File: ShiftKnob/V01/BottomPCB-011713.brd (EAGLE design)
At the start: 35.6 x 37.8 mm, 39 parts, among them IC2 7805DT, Q1 16MHz, Q2 MOSFET-NCHANNELSMD, Q3 MOSFET-NCHANNELSMD, Q4 MOSFET-NCHANNELSMD, Q5 MOSFET-NCHANNELSMD, Q6 MOSFET-NCHANNELSMD, U1 ATMEGA328

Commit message: adjust silk screen layer for large font size.
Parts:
- moved U$11 5.91 mm to (16.8, 25.8)
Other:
- board text added: "1-28-13"
- board text removed: "1-25-13"
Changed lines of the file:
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@@
 <grid distance="0.001" unitdist="inch" unit="inch" style="lines" multiple="1" display="yes" altdistance="0.025" altunitdist="inch" altunit="inch"/>
 <layers>
-<layer number="1" name="Top" color="4" fill="1" visible="yes" active="yes"/>
-<layer number="16" name="Bottom" color="1" fill="1" visible="yes" active="yes"/>
+<layer number="1" name="Top" color="4" fill="1" visible="no" active="yes"/>
+<layer number="16" name="Bottom" color="1" fill="1" visible="no" active="yes"/>
 <layer number="17" name="Pads" color="2" fill="1" visible="yes" active="yes"/>
 <layer number="18" name="Vias" color="2" fill="1" visible="yes" active="yes"/>
 <layer number="19" name="Unrouted" color="6" fill="1" visible="yes" active="yes"/>
 <layer number="20" name="Dimension" color="15" fill="1" visible="yes" active="yes"/>
-<layer number="21" name="tPlace" color="7" fill="1" visible="yes" active="yes"/>
+<layer number="21" name="tPlace" color="7" fill="1" visible="no" active="yes"/>
 <layer number="22" name="bPlace" color="6" fill="1" visible="yes" active="yes"/>
 <layer number="23" name="tOrigins" color="15" fill="1" visible="yes" active="yes"/>
@@
 <text x="31.2318" y="31.6128" size="0.8128" layer="21">RGB
  LED</text>
-<text x="23.053" y="19.116" size="1.016" layer="22" rot="MR90">ZNELSON1</text>
-<text x="21.529" y="20.005" size="1.016" layer="22" rot="MR90">1-25-13</text>
+<text x="22.037" y="19.6748" size="1.778" layer="22" rot="MR90">ZNELSON1</text>
+<text x="16.4998" y="10.4038" size="1.778" layer="22" rot="MR90">1-28-13</text>
 <rectangle x1="13.3756" y1="22.3672" x2="13.9852" y2="22.3926" layer="22" rot="R90"/>
 <rectangle x1="13.0073" y1="22.3545" x2="14.4043" y2="22.3799" layer="22" rot="R90"/>
@@
 <element name="C3" library="SparkFun" package="0402-CAP" value="0.1uF" x="27.244" y="31.308" rot="R45"/>
 <element name="C1" library="SparkFun" package="0402-CAP" value="0.1uF" x="17.338" y="25.212" rot="R135"/>
-<element name="U$11" library="SparkFun" package="SFE-LOGO-FLAME" value="LOGO-SFESK" x="16.322" y="19.878" smashed="yes" rot="MR90"/>
+<element name="U$11" library="SparkFun" package="SFE-LOGO-FLAME" value="LOGO-SFESK" x="16.7792" y="25.7708" smashed="yes" rot="MR90"/>
 <element name="Q1" library="SparkFun" package="RESONATOR-SMD" value="16MHz" x="24.577" y="36.9722" rot="R345"/>
 <element name="U1" library="SparkFun" package="TQFP32-08" value="ATMEGA328" x="20.005" y="31.181" rot="R225"/>

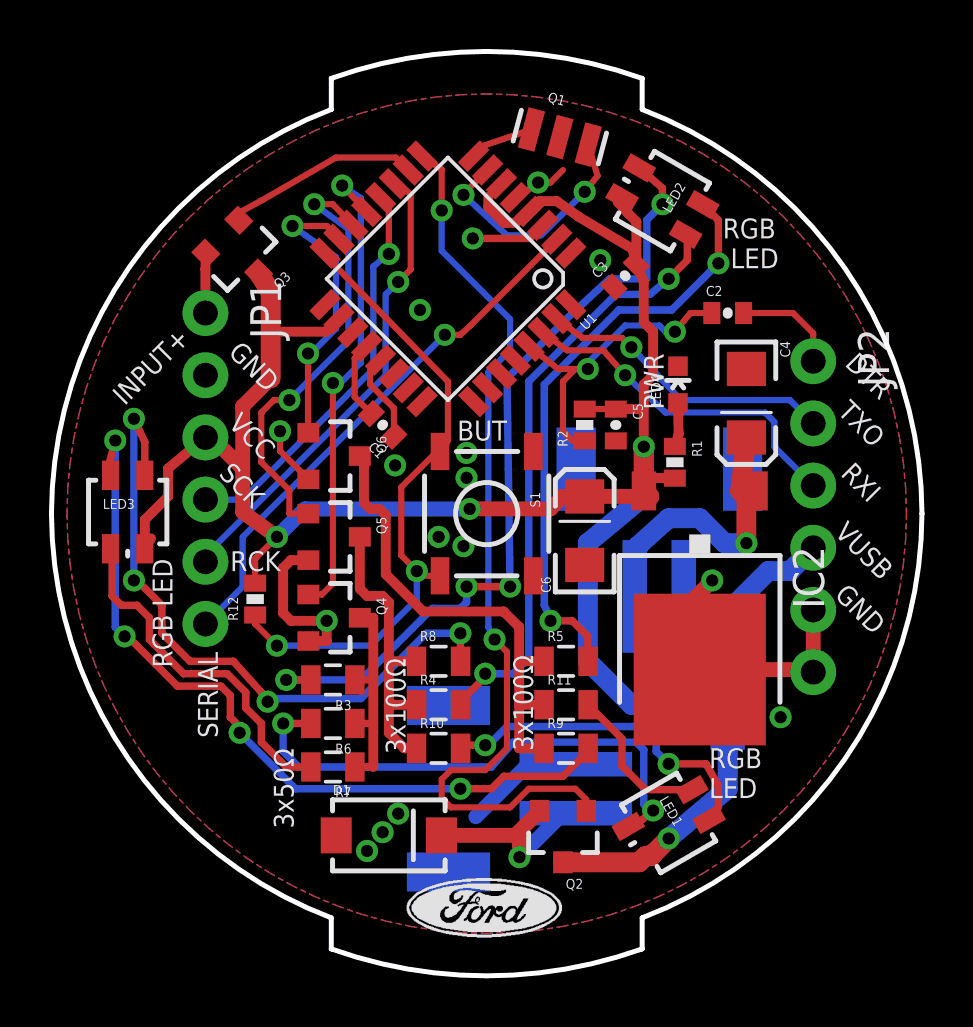
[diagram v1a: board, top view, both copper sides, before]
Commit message: run DRC test and fix all issues.
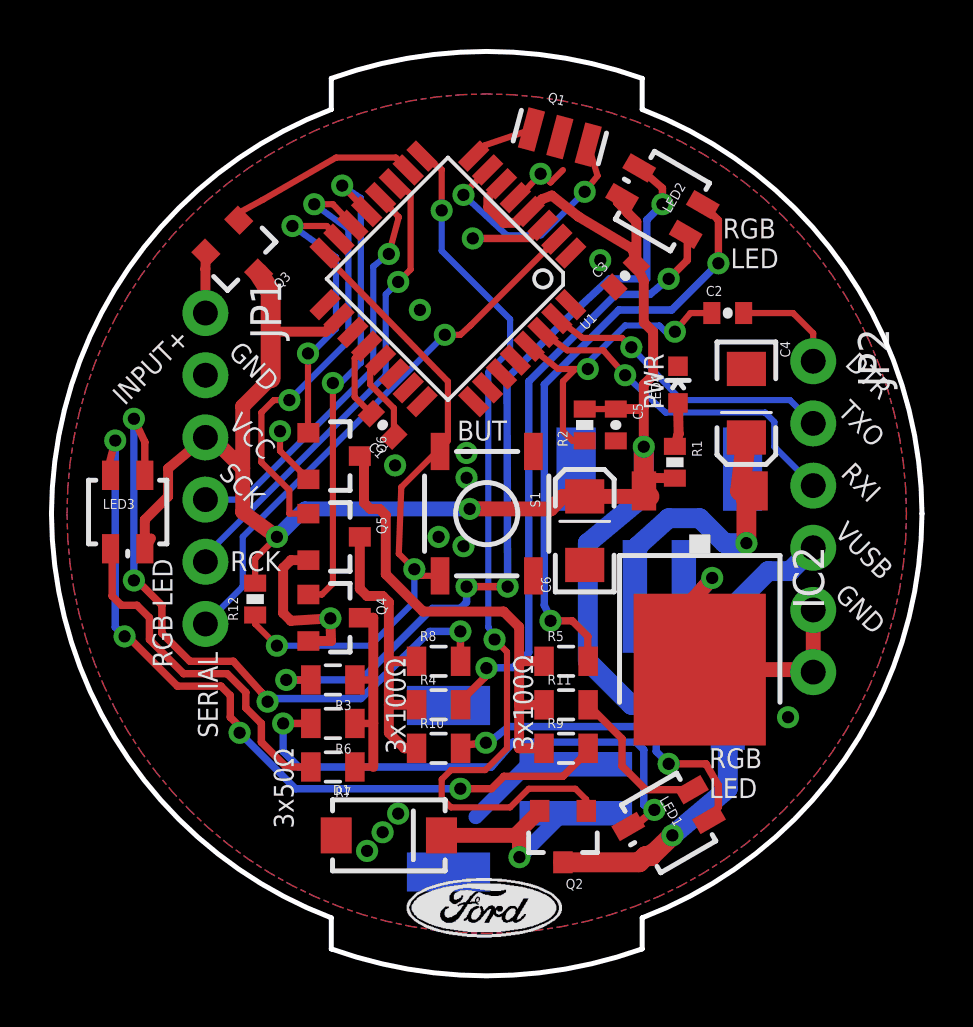
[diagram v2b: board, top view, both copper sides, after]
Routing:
- net GND: track 35.6 -> 36.6 mm

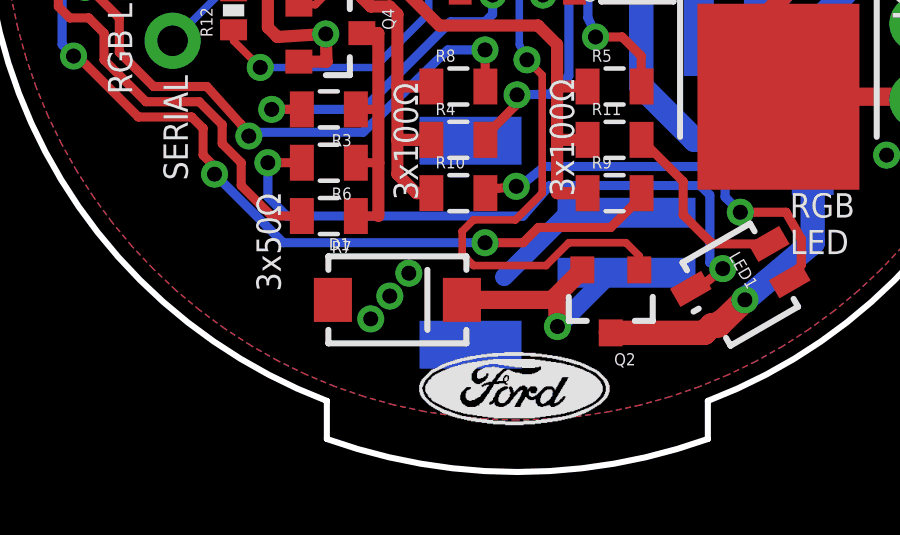
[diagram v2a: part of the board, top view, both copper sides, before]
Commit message: change diodes to match. add silk screen for polarity marking.
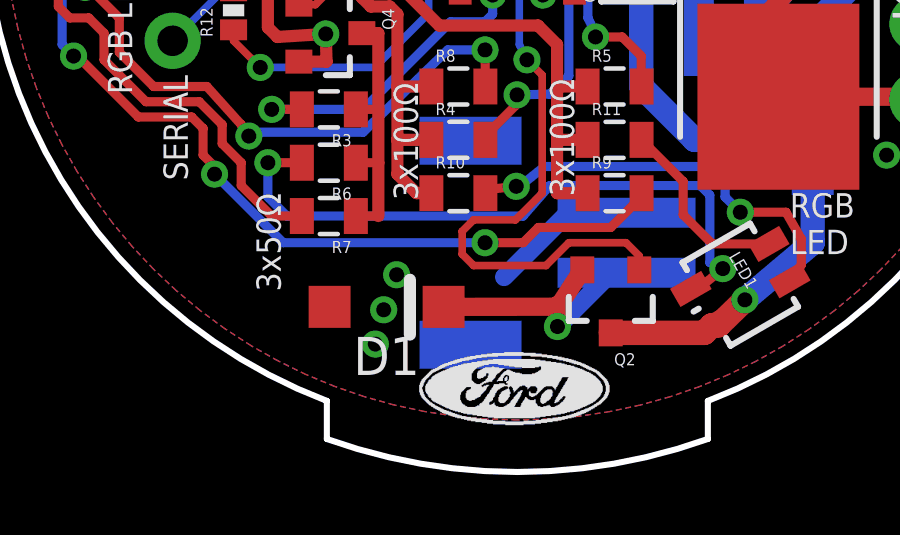
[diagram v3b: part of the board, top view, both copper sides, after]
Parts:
- D1: value MBRA140 -> MBR0520LT; device SparkFun-DiscreteSemi:SMA-DIODE -> diode:SOD123
- moved D1 0.43 mm to (17.2, 8.21), turned to 180 degrees
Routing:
- net MOTOR+: track 8.43 -> 9.12 mm
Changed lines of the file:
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@@
 <layer number="45" name="Holes" color="7" fill="1" visible="yes" active="yes"/>
 <layer number="46" name="Milling" color="3" fill="1" visible="no" active="yes"/>
-<layer number="47" name="Measures" color="7" fill="1" visible="no" active="yes"/>
+<layer number="47" name="Measures" color="7" fill="1" visible="yes" active="yes"/>
 <layer number="48" name="Document" color="7" fill="1" visible="no" active="yes"/>
 <layer number="49" name="Reference" color="7" fill="1" visible="no" active="yes"/>
@@
 <rectangle x1="20.7543" y1="6.6573" x2="22.2021" y2="6.6827" layer="21"/>
 <rectangle x1="21.1607" y1="6.6827" x2="21.7957" y2="6.7081" layer="21"/>
+<wire x1="30.2006" y1="13.8684" x2="32.6644" y2="13.8684" width="0.4064" layer="22"/>
+<wire x1="18.0086" y1="7.2898" x2="18.0086" y2="9.1186" width="0.4064" layer="21"/>
 </plain>
 <attributes>
@@
 <attribute name="PROD_ID" value="CONN-08352" x="21.529" y="10.353" size="1.778" layer="28" rot="MR270" display="off"/>
 </element>
-<element name="D1" library="SparkFun-DiscreteSemi" package="SMA-DIODE" value="MBRA140" x="17.592" y="8.448">
-<attribute name="PROD_ID" value="DIO-08053" x="17.592" y="8.448" size="1.778" layer="27" display="off"/>
-</element>
+<element name="D1" library="diode" package="SOD123" value="MBR0520LT" x="17.2314" y="8.2144" rot="R180"/>
 <element name="LED1" library="SparkFun" package="LED-TRICOLOR-SMD" value="LED-TRICOLOR" x="29.022" y="8.956" rot="R300"/>
 <element name="R6" library="SparkFun-Resistors" package="0805" value="50" x="15.306" y="13.02" rot="R180"/>
@@
 <wire x1="23.7896" y1="35.4736" x2="24.196" y2="35.118" width="0.254" layer="1"/>
 <wire x1="24.196" y1="35.118" x2="24.704" y2="35.626" width="0.254" layer="1"/>
-<via x="16.703" y="7.813" extent="1-16" drill="0.5"/>
-<via x="17.338" y="8.575" extent="1-16" drill="0.5"/>
-<via x="17.973" y="9.337" extent="1-16" drill="0.5"/>
+<via x="16.8554" y="6.9748" extent="1-16" drill="0.5"/>
+<via x="17.1348" y="8.1178" extent="1-16" drill="0.5"/>
+<via x="17.5666" y="9.2862" extent="1-16" drill="0.5"/>
 <wire x1="23.888853125" y1="33.367796875" x2="23.35305625" y2="32.832" width="0.3048" layer="1"/>
 <wire x1="23.35305625" y1="32.832" x2="21.021" y2="32.832" width="0.3048" layer="1"/>
@@
 <contactref element="JP4" pad="2"/>
 <contactref element="D1" pad="C"/>
-<wire x1="19.742" y1="8.448" x2="22.754" y2="8.448" width="0.6096" layer="1"/>
-<wire x1="22.754" y1="8.448" x2="23.754" y2="9.448" width="0.6096" layer="1"/>
+<wire x1="19.1314" y1="8.2144" x2="22.9572" y2="8.2194" width="0.6096" layer="1"/>
+<wire x1="22.9572" y1="8.2194" x2="23.754" y2="9.448" width="0.6096" layer="1"/>
 <wire x1="25.229" y1="9.353" x2="24.72" y2="9.353" width="0.6096" layer="16"/>
 <wire x1="24.72" y1="9.353" x2="22.926" y2="7.559" width="0.6096" layer="16"/>
 <via x="22.926" y="7.559" extent="1-16" drill="0.5" diameter="0.4064"/>
 <wire x1="22.926" y1="7.559" x2="22.926" y2="8.276" width="0.6096" layer="1"/>
-<wire x1="22.926" y1="8.276" x2="22.754" y2="8.448" width="0.6096" layer="1"/>
+<wire x1="22.926" y1="8.276" x2="22.9572" y2="8.2194" width="0.6096" layer="1"/>
 </signal>
 <signal name="N$7">
